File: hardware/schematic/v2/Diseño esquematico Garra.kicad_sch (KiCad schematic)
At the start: 18 parts

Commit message: feat: PCB routing first stage completed
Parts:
- renumbered Bornier_N20_DC to Bornier_N20_DC1
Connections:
- net B_DWN: now also CIAA-P2.36 (GPIO5)
- net B_UP: now also CIAA-P2.38 (GPIO7)
- net IN1: now also CIAA-P1.35 (TFIL3); no longer CIAA-P1.33 (TFIL0)
- net IN2: now also CIAA-P1.33 (TFIL0); no longer CIAA-P1.35 (TFIL3)
- net SW: now also CIAA-P2.40 (GPIO8)
- net TFIL2 renamed SERVO_PWM
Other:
- moved on the sheet: Bornier_N20_DC1
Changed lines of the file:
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@@
 	(wire
 		(pts
-			(xy 182.88 127) (xy 187.96 127)
+			(xy 264.16 146.05) (xy 269.24 146.05)
 		)
 		(stroke
@@
 	(wire
 		(pts
-			(xy 233.68 146.05) (xy 238.76 146.05)
+			(xy 182.88 127) (xy 187.96 127)
 		)
 		(stroke
@@
 	(wire
 		(pts
-			(xy 264.16 146.05) (xy 269.24 146.05)
+			(xy 233.68 146.05) (xy 238.76 146.05)
 		)
 		(stroke
@@
 	(wire
 		(pts
-			(xy 152.4 60.96) (xy 157.48 60.96)
+			(xy 149.86 60.96) (xy 154.94 60.96)
 		)
 		(stroke
@@
 	(wire
 		(pts
-			(xy 233.68 105.41) (xy 238.76 105.41)
+			(xy 264.16 143.51) (xy 269.24 143.51)
 		)
 		(stroke
@@
 	(wire
 		(pts
-			(xy 48.26 139.7) (xy 48.26 135.89)
+			(xy 233.68 105.41) (xy 238.76 105.41)
 		)
 		(stroke
@@
 	(wire
 		(pts
-			(xy 233.68 49.53) (xy 238.76 49.53)
+			(xy 48.26 139.7) (xy 48.26 135.89)
 		)
 		(stroke
@@
 	(wire
 		(pts
-			(xy 233.68 31.75) (xy 238.76 31.75)
+			(xy 233.68 49.53) (xy 238.76 49.53)
 		)
 		(stroke
@@
 	(wire
 		(pts
-			(xy 172.72 35.56) (xy 175.26 35.56)
+			(xy 233.68 31.75) (xy 238.76 31.75)
 		)
 		(stroke
@@
 	(wire
 		(pts
-			(xy 264.16 148.59) (xy 269.24 148.59)
+			(xy 172.72 35.56) (xy 175.26 35.56)
 		)
 		(stroke
@@
 	(wire
 		(pts
-			(xy 152.4 63.5) (xy 157.48 63.5)
+			(xy 149.86 63.5) (xy 154.94 63.5)
 		)
 		(stroke
@@
 	(wire
 		(pts
-			(xy 233.68 140.97) (xy 238.76 140.97)
+			(xy 264.16 148.59) (xy 269.24 148.59)
 		)
 		(stroke
@@
 	(wire
 		(pts
-			(xy 269.24 59.69) (xy 264.16 59.69)
+			(xy 233.68 140.97) (xy 238.76 140.97)
 		)
 		(stroke
@@
 	(wire
 		(pts
-			(xy 30.48 107.95) (xy 35.56 107.95)
+			(xy 269.24 59.69) (xy 264.16 59.69)
 		)
 		(stroke
@@
 	(wire
 		(pts
-			(xy 30.48 118.11) (xy 35.56 118.11)
+			(xy 30.48 107.95) (xy 35.56 107.95)
 		)
 		(stroke
@@
 	(wire
 		(pts
-			(xy 233.68 64.77) (xy 238.76 64.77)
+			(xy 30.48 118.11) (xy 35.56 118.11)
 		)
 		(stroke
@@
 	(wire
 		(pts
-			(xy 30.48 110.49) (xy 35.56 110.49)
+			(xy 233.68 64.77) (xy 238.76 64.77)
 		)
 		(stroke
@@
 	(wire
 		(pts
-			(xy 233.68 115.57) (xy 238.76 115.57)
+			(xy 30.48 110.49) (xy 35.56 110.49)
 		)
 		(stroke
@@
 	(wire
 		(pts
-			(xy 264.16 143.51) (xy 269.24 143.51)
+			(xy 233.68 115.57) (xy 238.76 115.57)
 		)
 		(stroke
@@
 		)
 	)
-	(global_label "B_UP"
+	(global_label "MOTOR_VCC"
 		(shape output)
-		(at 276.86 146.05 180)
+		(at 144.78 30.48 180)
 		(effects
 			(font
@@
 		)
 		(property "Intersheetrefs" "${INTERSHEET_REFS}"
-			(at 276.86 146.05 0)
+			(at 144.78 30.48 0)
 			(effects
 				(font
@@
 		)
 	)
-	(global_label "MOTOR_VCC"
-		(shape output)
-		(at 144.78 30.48 180)
+	(global_label "GND"
+		(shape input)
+		(at 269.24 67.31 0)
 		(effects
 			(font
 				(size 1.27 1.27)
 			)
-			(justify right)
+			(justify left)
 		)
 		(property "Intersheetrefs" "${INTERSHEET_REFS}"
-			(at 144.78 30.48 0)
+			(at 269.24 67.31 0)
 			(effects
 				(font
@@
 		)
 	)
-	(global_label "GND"
+	(global_label "GND_B_UP"
 		(shape input)
-		(at 269.24 67.31 0)
+		(at 182.88 123.19 180)
 		(effects
 			(font
 				(size 1.27 1.27)
 			)
-			(justify left)
+			(justify right)
 		)
 		(property "Intersheetrefs" "${INTERSHEET_REFS}"
-			(at 269.24 67.31 0)
+			(at 182.88 123.19 0)
 			(effects
 				(font
@@
 		)
 	)
-	(global_label "GND_B_UP"
+	(global_label "SW"
 		(shape input)
-		(at 182.88 123.19 180)
+		(at 269.24 148.59 0)
 		(effects
 			(font
 				(size 1.27 1.27)
 			)
-			(justify right)
+			(justify left)
 		)
 		(property "Intersheetrefs" "${INTERSHEET_REFS}"
-			(at 182.88 123.19 0)
+			(at 269.24 148.59 0)
 			(effects
 				(font
 					(size 1.27 1.27)
 				)
+				(justify left)
 				(hide yes)
 			)
@@
 		)
 	)
-	(global_label "B_DWN"
-		(shape output)
-		(at 278.13 143.51 180)
-		(effects
-			(font
-				(size 1.27 1.27)
-			)
-			(justify right)
-		)
-		(property "Intersheetrefs" "${INTERSHEET_REFS}"
-			(at 278.13 143.51 0)
-			(effects
-				(font
-					(size 1.27 1.27)
-				)
-				(hide yes)
-			)
-		)
-	)
 	(global_label "GND"
 		(shape input)
@@
 	(global_label "MOTOR_GND"
 		(shape input)
-		(at 157.48 63.5 0)
+		(at 154.94 63.5 0)
 		(effects
 			(font
@@
 		)
 		(property "Intersheetrefs" "${INTERSHEET_REFS}"
-			(at 157.48 63.5 0)
+			(at 154.94 63.5 0)
 			(effects
 				(font
@@
 		)
 	)
-	(global_label "TFIL2"
+	(global_label "SERVO_PWM"
 		(shape output)
 		(at 233.68 67.31 180)
@@
 		)
 	)
-	(global_label "SW"
-		(shape output)
-		(at 274.32 148.59 180)
-		(effects
-			(font
-				(size 1.27 1.27)
-			)
-			(justify right)
-		)
-		(property "Intersheetrefs" "${INTERSHEET_REFS}"
-			(at 274.32 148.59 0)
-			(effects
-				(font
-					(size 1.27 1.27)
-				)
-				(hide yes)
-			)
-		)
-	)
 	(global_label "M02"
 		(shape input)
@@
 		)
 	)
-	(global_label "TFIL2"
+	(global_label "B_DWN"
+		(shape input)
+		(at 269.24 143.51 0)
+		(effects
+			(font
+				(size 1.27 1.27)
+			)
+			(justify left)
+		)
+		(property "Intersheetrefs" "${INTERSHEET_REFS}"
+			(at 269.24 143.51 0)
+			(effects
+				(font
+					(size 1.27 1.27)
+				)
+				(justify left)
+				(hide yes)
+			)
+		)
+	)
+	(global_label "SERVO_PWM"
 		(shape input)
 		(at 184.15 63.5 180)
@@
 		)
 	)
-	(global_label "IN2"
+	(global_label "IN1"
 		(shape output)
 		(at 233.68 64.77 180)
@@
 	(global_label "MOTOR_VCC"
 		(shape input)
-		(at 157.48 60.96 0)
+		(at 154.94 60.96 0)
 		(effects
 			(font
@@
 		)
 		(property "Intersheetrefs" "${INTERSHEET_REFS}"
-			(at 157.48 60.96 0)
+			(at 154.94 60.96 0)
 			(effects
 				(font
@@
 		)
 	)
+	(global_label "B_UP"
+		(shape input)
+		(at 269.24 146.05 0)
+		(effects
+			(font
+				(size 1.27 1.27)
+			)
+			(justify left)
+		)
+		(property "Intersheetrefs" "${INTERSHEET_REFS}"
+			(at 269.24 146.05 0)
+			(effects
+				(font
+					(size 1.27 1.27)
+				)
+				(justify left)
+				(hide yes)
+			)
+		)
+	)
 	(global_label "A2_2"
 		(shape input)
@@
 		)
 	)
-	(global_label "IN1"
+	(global_label "IN2"
 		(shape output)
 		(at 233.68 62.23 180)
@@
 	(symbol
 		(lib_id "Connector:Screw_Terminal_01x02")
-		(at 147.32 60.96 0)
+		(at 144.78 60.96 0)
 		(mirror y)
 		(unit 1)
@@
 		(on_board yes)
 		(dnp no)
-		(property "Reference" "Bornier_N20_DC"
-			(at 144.78 61.468 0)
+		(property "Reference" "Bornier_N20_DC1"
+			(at 142.24 61.468 0)
 			(effects
 				(font
@@
 		)
 		(property "Value" "Screw_Terminal_01x05"
-			(at 144.78 64.008 0)
+			(at 142.24 64.008 0)
 			(effects
 				(font
@@
 		)
 		(property "Footprint" "TerminalBlock_Phoenix:TerminalBlock_Phoenix_MKDS-1,5-2-5.08_1x02_P5.08mm_Horizontal"
-			(at 147.32 60.96 0)
+			(at 144.78 60.96 0)
 			(effects
 				(font
@@
 		)
 		(property "Datasheet" "~"
-			(at 147.32 60.96 0)
+			(at 144.78 60.96 0)
 			(effects
 				(font
@@
 		)
 		(property "Description" "Generic screw terminal, single row, 01x02, script generated (kicad-library-utils/schlib/autogen/connector/)"
-			(at 147.32 60.96 0)
+			(at 144.78 60.96 0)
 			(effects
 				(font
@@
 			(project "Diseño esquematico Garra"
 				(path "/a88248f6-7b70-4a9d-b538-4e8e42a3a066"
-					(reference "Bornier_N20_DC")
+					(reference "Bornier_N20_DC1")
 					(unit 1)
 				)

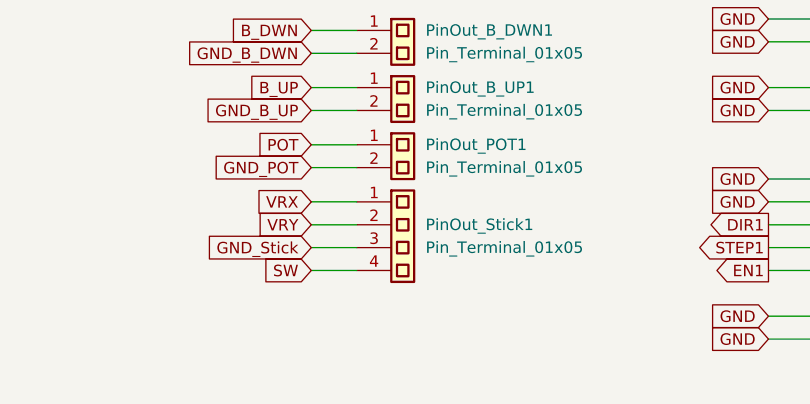
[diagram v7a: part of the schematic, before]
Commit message: docs: Schematics PDF added
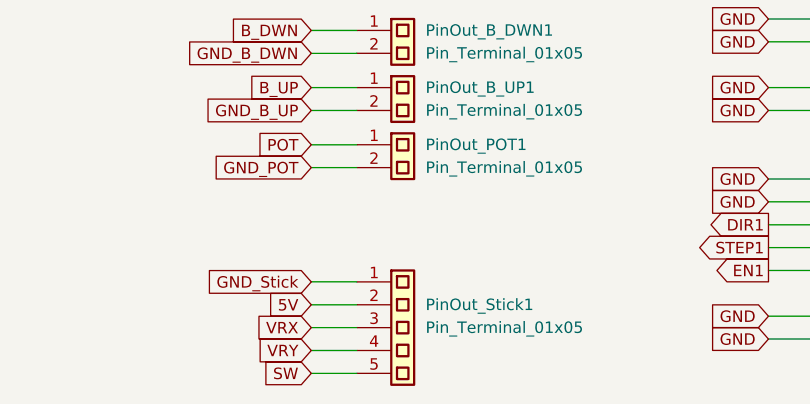
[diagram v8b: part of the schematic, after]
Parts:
- PinOut_Stick1: footprint Connector_PinSocket_2.00mm:PinSocket_1x04_P2.00mm_Vertical -> Connector_PinSocket_2.00mm:PinSocket_1x05_P2.00mm_Vertical
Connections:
- net 5V: now also PinOut_Stick1.2 (Pin_2)
- net GND_Stick: now also PinOut_Stick1.1 (Pin_1); no longer PinOut_Stick1.3 (Pin_3)
- net SW: now also PinOut_Stick1.5 (Pin_5); no longer PinOut_Stick1.4 (Pin_4)
- net VRX: now also PinOut_Stick1.3 (Pin_3); no longer PinOut_Stick1.1 (Pin_1)
- net VRY: now also PinOut_Stick1.4 (Pin_4); no longer PinOut_Stick1.2 (Pin_2)
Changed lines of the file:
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@@
 	(wire
 		(pts
+			(xy 182.88 152.4) (xy 187.96 152.4)
+		)
+		(stroke
+			(width 0)
+			(type default)
+		)
+	)
+	(wire
+		(pts
 			(xy 71.12 86.36) (xy 80.01 86.36)
 		)
@@
 	(wire
 		(pts
+			(xy 182.88 144.78) (xy 187.96 144.78)
+		)
+		(stroke
+			(width 0)
+			(type default)
+		)
+	)
+	(wire
+		(pts
 			(xy 30.48 40.64) (xy 35.56 40.64)
 		)
@@
 	(wire
 		(pts
-			(xy 182.88 127) (xy 187.96 127)
+			(xy 182.88 149.86) (xy 187.96 149.86)
 		)
 		(stroke
@@
 	(wire
 		(pts
-			(xy 233.68 146.05) (xy 238.76 146.05)
+			(xy 182.88 127) (xy 187.96 127)
 		)
 		(stroke
@@
 	(wire
 		(pts
-			(xy 45.72 96.52) (xy 45.72 100.33)
+			(xy 233.68 146.05) (xy 238.76 146.05)
 		)
 		(stroke
@@
 	(wire
 		(pts
-			(xy 269.24 52.07) (xy 264.16 52.07)
+			(xy 45.72 96.52) (xy 45.72 100.33)
 		)
 		(stroke
@@
 	(wire
 		(pts
-			(xy 71.12 81.28) (xy 80.01 81.28)
+			(xy 269.24 52.07) (xy 264.16 52.07)
 		)
 		(stroke
@@
 	(wire
 		(pts
-			(xy 182.88 138.43) (xy 187.96 138.43)
+			(xy 71.12 81.28) (xy 80.01 81.28)
 		)
 		(stroke
@@
 	(wire
 		(pts
-			(xy 182.88 135.89) (xy 187.96 135.89)
-		)
-		(stroke
-			(width 0)
-			(type default)
-		)
-	)
-	(wire
-		(pts
 			(xy 149.86 60.96) (xy 154.94 60.96)
 		)
@@
 	(wire
 		(pts
-			(xy 182.88 133.35) (xy 187.96 133.35)
+			(xy 71.12 93.98) (xy 80.01 93.98)
 		)
 		(stroke
@@
 	(wire
 		(pts
-			(xy 71.12 93.98) (xy 80.01 93.98)
+			(xy 149.86 63.5) (xy 154.94 63.5)
 		)
 		(stroke
@@
 	(wire
 		(pts
-			(xy 149.86 63.5) (xy 154.94 63.5)
+			(xy 184.15 52.07) (xy 189.23 52.07)
 		)
 		(stroke
@@
 	(wire
 		(pts
-			(xy 184.15 52.07) (xy 189.23 52.07)
+			(xy 30.48 125.73) (xy 35.56 125.73)
 		)
 		(stroke
@@
 	(wire
 		(pts
-			(xy 30.48 125.73) (xy 35.56 125.73)
+			(xy 80.01 73.66) (xy 93.98 73.66)
 		)
 		(stroke
@@
 	(wire
 		(pts
-			(xy 80.01 73.66) (xy 93.98 73.66)
+			(xy 269.24 140.97) (xy 264.16 140.97)
 		)
 		(stroke
@@
 	(wire
 		(pts
-			(xy 269.24 140.97) (xy 264.16 140.97)
+			(xy 182.88 142.24) (xy 187.96 142.24)
 		)
 		(stroke
@@
 	(wire
 		(pts
-			(xy 182.88 140.97) (xy 187.96 140.97)
+			(xy 182.88 147.32) (xy 187.96 147.32)
 		)
 		(stroke
@@
 	(global_label "SW"
 		(shape input)
-		(at 182.88 140.97 180)
+		(at 182.88 152.4 180)
 		(effects
 			(font
@@
 		)
 		(property "Intersheetrefs" "${INTERSHEET_REFS}"
-			(at 182.88 140.97 0)
+			(at 182.88 152.4 0)
 			(effects
 				(font
@@
 	(global_label "GND_Stick"
 		(shape input)
-		(at 182.88 138.43 180)
+		(at 182.88 142.24 180)
 		(effects
 			(font
@@
 		)
 		(property "Intersheetrefs" "${INTERSHEET_REFS}"
-			(at 182.88 138.43 0)
+			(at 182.88 142.24 0)
 			(effects
 				(font
@@
 		)
 	)
+	(global_label "5V"
+		(shape input)
+		(at 182.88 144.78 180)
+		(effects
+			(font
+				(size 1.27 1.27)
+			)
+			(justify right)
+		)
+		(property "Intersheetrefs" "${INTERSHEET_REFS}"
+			(at 182.88 144.78 0)
+			(effects
+				(font
+					(size 1.27 1.27)
+				)
+				(hide yes)
+			)
+		)
+	)
 	(global_label "12V"
 		(shape input)
@@
 	(global_label "VRY"
 		(shape input)
-		(at 182.88 135.89 180)
+		(at 182.88 149.86 180)
 		(effects
 			(font
@@
 		)
 		(property "Intersheetrefs" "${INTERSHEET_REFS}"
-			(at 182.88 135.89 0)
+			(at 182.88 149.86 0)
 			(effects
 				(font
@@
 	(global_label "VRX"
 		(shape input)
-		(at 182.88 133.35 180)
+		(at 182.88 147.32 180)
 		(effects
 			(font
@@
 		)
 		(property "Intersheetrefs" "${INTERSHEET_REFS}"
-			(at 182.88 133.35 0)
+			(at 182.88 147.32 0)
 			(effects
 				(font
@@
 		(lib_name "Screw_Terminal_01x02_2")
 		(lib_id "Connector:Screw_Terminal_01x02")
-		(at 193.04 133.35 0)
+		(at 193.04 142.24 0)
 		(unit 1)
 		(exclude_from_sim no)
@@
 		(fields_autoplaced yes)
 		(property "Reference" "PinOut_Stick1"
-			(at 195.58 135.8899 0)
+			(at 195.58 144.7799 0)
 			(effects
 				(font
@@
 		)
 		(property "Value" "Pin_Terminal_01x05"
-			(at 195.58 138.4299 0)
+			(at 195.58 147.3199 0)
 			(effects
 				(font
@@
 			)
 		)
-		(property "Footprint" "Connector_PinSocket_2.00mm:PinSocket_1x04_P2.00mm_Vertical"
-			(at 193.294 128.016 0)
+		(property "Footprint" "Connector_PinSocket_2.00mm:PinSocket_1x05_P2.00mm_Vertical"
+			(at 193.294 136.906 0)
 			(effects
 				(font
@@
 		)
 		(property "Datasheet" "~"
-			(at 193.04 144.272 0)
+			(at 193.04 153.162 0)
 			(effects
 				(font
@@
 		)
 		(property "Description" "Generic screw terminal, single row, 01x02, script generated (kicad-library-utils/schlib/autogen/connector/)"
-			(at 193.802 145.288 0)
+			(at 193.802 154.178 0)
 			(effects
 				(font
@@
 		(pin "4"
 		)
+		(pin "5"
+		)
 		(instances
